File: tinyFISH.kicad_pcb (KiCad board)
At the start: 2 copper layers, 20 x 20 mm, 88 parts, among them Q1 SI2302DS, U1 CC2510, U2 MPU-6000, U3 LP2985AIM5-3.0/NOPB, U4 STM32F303CCTx, U5 M25P16-VME, U6 MICRO_USB_B, U7 INA139, X1 26MHz, X2 8MHz

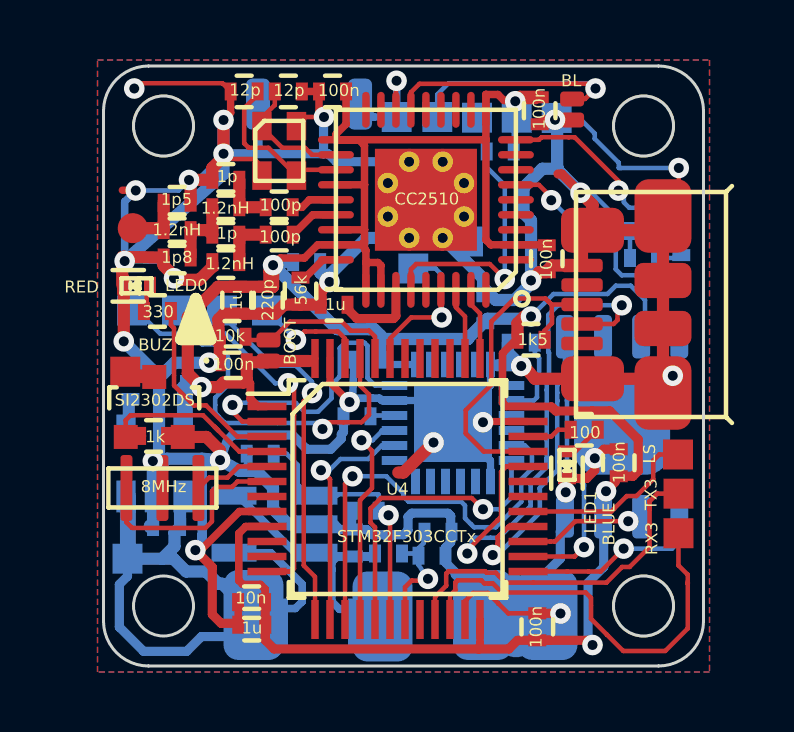
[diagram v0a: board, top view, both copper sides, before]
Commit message: some cosmetic cleanup, fixed esc4 naming
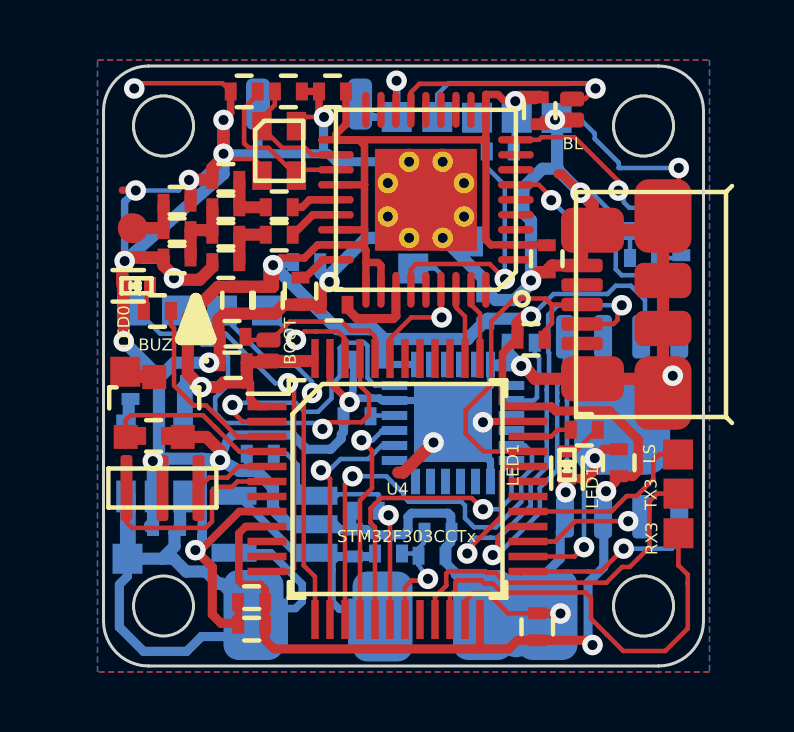
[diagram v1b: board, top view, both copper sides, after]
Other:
- board text removed: "LED0"

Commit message: swapped blue and red led
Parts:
- LED0: value RED -> BLUE
- LED1: value BLUE -> RED
- R7: value 330 -> 100
- R8: value 100 -> 330

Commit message: cleanup and added 3d shapes
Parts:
- LED0: value BLUE -> RED
- LED1: value RED -> BLUE
- R7: value 100 -> 330
- R8: value 330 -> 100
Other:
- board text added: "ESC 4"
- board text removed: "ESC 0"

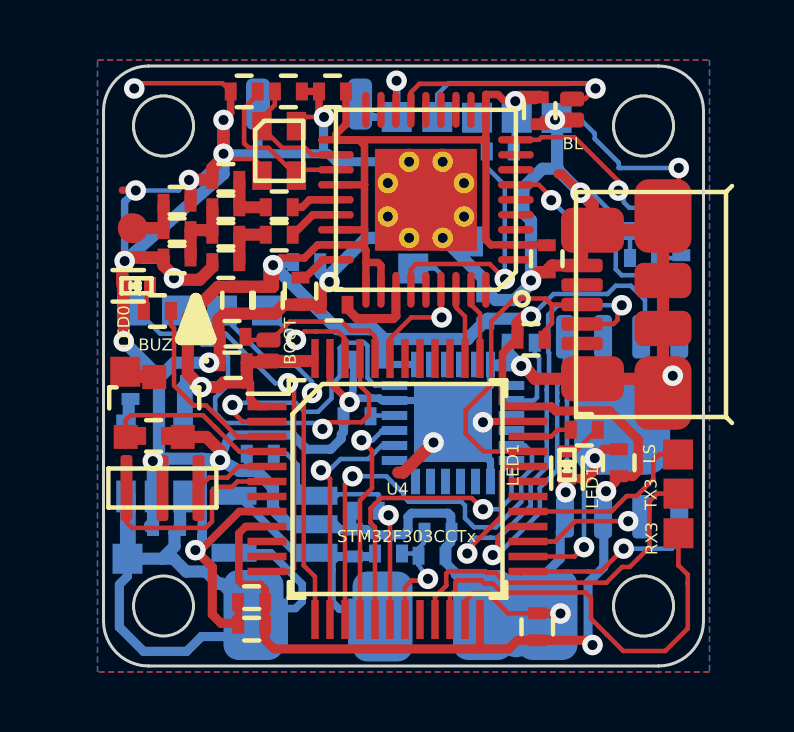
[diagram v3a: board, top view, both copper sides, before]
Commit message: cleanup to custom r and c parts
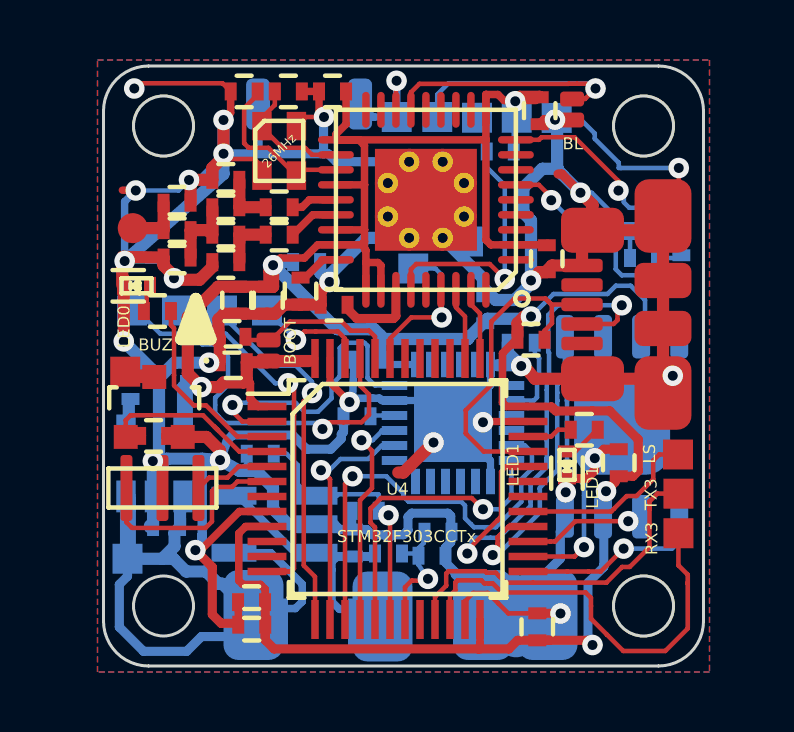
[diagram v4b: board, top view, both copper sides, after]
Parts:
- C1, C10, C11, C12, C13, C14, C15, C16, C17, C18, C19, C2, C20, C21, C22, C23, C24, C25, C26, C27, C28, C29, C3, C30, C4, C5, C6, C7, C8, C9: footprint Resistors_SMD:R_0402 -> custom:C_0402_CUSTOM
- L1, L2, L3: footprint Resistors_SMD:R_0402 -> custom:L_0402_CUSTOM
- LED0: value RED -> BLUE
- LED1: value BLUE -> RED
- R1, R10, R11, R13, R3, R4, R5, R501, R6, R9: footprint Resistors_SMD:R_0402 -> custom:R_0402_CUSTOM
- R7: value 330 -> 100; footprint Resistors_SMD:R_0402 -> custom:R_0402_CUSTOM
- R8: value 100 -> 330; footprint Resistors_SMD:R_0402 -> custom:R_0402_CUSTOM
